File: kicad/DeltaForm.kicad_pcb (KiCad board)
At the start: 2 copper layers, 85.4 x 128.6 mm, 66 parts

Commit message: added MCU
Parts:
- moved D1 270.0 mm to (443.8, 98.5)
- moved D10 270.0 mm to (462.9, 141.4)
- moved D11 270.0 mm to (481.9, 141.4)
- moved D12 270.0 mm to (443.8, 160.4)
- moved D13 270.0 mm to (462.9, 160.4)
- moved D14 270.0 mm to (481.9, 160.4)
- moved D15 270.0 mm to (443.8, 179.5)
- moved D16 270.0 mm to (462.9, 179.5)
- moved D17 270.0 mm to (481.9, 179.5)
- moved D18 270.0 mm to (481.9, 198.5)
- moved D19 270.0 mm to (500.9, 150.9)
- moved D2 270.0 mm to (443.8, 122.3)
- moved D20 270.0 mm to (500.9, 189.0)
- moved D21 270.0 mm to (453.3, 198.5)
- moved D3 270.0 mm to (462.9, 98.5)
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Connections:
- S1 pad 1: col_3 -> Net-(D1-A)
- S1 pad 2: Net-(D1-A) -> col_3
- S10 pad 1: col_4 -> Net-(D10-A)
- S10 pad 2: Net-(D10-A) -> col_4
- S11 pad 1: col_5 -> Net-(D11-A)
- S11 pad 2: Net-(D11-A) -> col_5
- S12 pad 1: col_3 -> Net-(D12-A)
- S12 pad 2: Net-(D12-A) -> col_3
- S13 pad 1: col_4 -> Net-(D13-A)
- S13 pad 2: Net-(D13-A) -> col_4
- S14 pad 1: col_5 -> Net-(D14-A)
- S14 pad 2: Net-(D14-A) -> col_5
- S15 pad 1: col_3 -> Net-(D15-A)
- S15 pad 2: Net-(D15-A) -> col_3
- S16 pad 1: col_4 -> Net-(D16-A)
- S16 pad 2: Net-(D16-A) -> col_4
- S17 pad 1: col_5 -> Net-(D17-A)
- S17 pad 2: Net-(D17-A) -> col_5
- S18 pad 1: col_5 -> Net-(D18-A)
- S18 pad 2: Net-(D18-A) -> col_5
- S19 pad 1: col_6 -> Net-(D19-A)
- S19 pad 2: Net-(D19-A) -> col_6
- S2 pad 1: col_3 -> Net-(D2-A)
- S2 pad 2: Net-(D2-A) -> col_3
- S20 pad 1: col_6 -> Net-(D20-A)
- S20 pad 2: Net-(D20-A) -> col_6
- S21 pad 1: col_3 -> Net-(D21-A)
- S21 pad 2: Net-(D21-A) -> col_3
- S3 pad 1: col_4 -> Net-(D3-A)
- S3 pad 2: Net-(D3-A) -> col_4
- S4 pad 1: col_4 -> Net-(D4-A)
- S4 pad 2: Net-(D4-A) -> col_4
- S5 pad 1: col_5 -> Net-(D5-A)
- S5 pad 2: Net-(D5-A) -> col_5
- S6 pad 1: col_5 -> Net-(D6-A)
- S6 pad 2: Net-(D6-A) -> col_5
- S7 pad 1: col_6 -> Net-(D7-A)
- S7 pad 2: Net-(D7-A) -> col_6
- S8 pad 1: col_6 -> Net-(D8-A)
- S8 pad 2: Net-(D8-A) -> col_6
- S9 pad 1: col_3 -> Net-(D9-A)
- S9 pad 2: Net-(D9-A) -> col_3
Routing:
- net GND: track 0.00 -> 441.7 mm, vias 0 -> 12
- net VCC: track 0.00 -> 429.4 mm, vias 0 -> 3
- net col_3: track 0.00 -> 123.9 mm
- net col_5: track 0.00 -> 116.8 mm
- net col_6: track 0.00 -> 102.1 mm
- net col_4: track 0.00 -> 98.7 mm
- net row_16: track 0.00 -> 80.2 mm, vias 0 -> 1
- net row_14: track 0.00 -> 73.5 mm, vias 0 -> 1
- net row_12: track 0.00 -> 61.0 mm
- net row_13: track 0.00 -> 42.2 mm
- net row_15: track 0.00 -> 21.9 mm
- net Net-(D17-A): track 0.00 -> 7.79 mm
- net Net-(D11-A): track 0.00 -> 7.79 mm
- net Net-(D6-A): track 0.00 -> 7.79 mm
- net Net-(D5-A): track 0.00 -> 7.79 mm
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
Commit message: updated MCU
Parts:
- D1, D10, D11, D12, D13, D14, D15, D16, D17, D18, D19, D2, D20, D21, D3, D4, D5, D6, D7, D8, D9: value 1N4148W -> (none)
- S1, S10, S11, S12, S13, S14, S15, S16, S17, S18, S19, S2, S20, S3, S4, S5, S6, S7, S8, S9: value SW_MX_HS -> (none)
- S21: value SW_MX_HS -> (none); footprint TB2086_KEYSWITCH:SW_MX_HS_2u -> TB2086_KEYSWITCH:SW_MX_HS_1u
- STB1, STB2, STB3: value MX_stab -> Stabilizer_Cherry_MX_2.00u
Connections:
- net Net-(D1-A) renamed c17_func
- net Net-(D10-A) renamed c18_top
- net Net-(D11-A) renamed c19_top
- net Net-(D12-A) renamed c17_home
- net Net-(D13-A) renamed c18_home
- net Net-(D14-A) renamed c19_home
- net Net-(D15-A) renamed c17_bottom
- net Net-(D16-A) renamed c18_bottom
- net Net-(D17-A) renamed c19_bottom
- net Net-(D18-A) renamed c18_thumb
- net Net-(D19-A) renamed c20_top
- net Net-(D2-A) renamed c17_number
- net Net-(D20-A) renamed c20_bottom
- net Net-(D21-A) renamed c17_thumb
- net Net-(D3-A) renamed c18_func
- net Net-(D4-A) renamed c18_number
- net Net-(D5-A) renamed c19_func
- net Net-(D6-A) renamed c19_number
- net Net-(D7-A) renamed c20_func
- net Net-(D8-A) renamed c20_number
- net Net-(D9-A) renamed c17_top
- net row_12 renamed function
- net row_13 renamed number
- net row_14 renamed top
- net row_15 renamed home
- net row_16 renamed bottom
- net row_17 renamed thumb
- S1 pad 2: col_3 -> col_1
- S10 pad 2: col_4 -> col_1
- S11 pad 2: col_5 -> col_4
- S12 pad 2: col_3 -> col_1
- S13 pad 2: col_4 -> col_1
- S14 pad 2: col_5 -> col_4
- S15 pad 2: col_3 -> col_1
- S16 pad 2: col_4 -> col_1
- S17 pad 2: col_5 -> col_4
- S18 pad 2: col_5 -> col_1
- S19 pad 2: col_6 -> col_3
- S2 pad 2: col_3 -> col_1
- S20 pad 2: col_6 -> col_3
- S21 pad 2: col_3 -> col_1
- S3 pad 2: col_4 -> col_1
- S4 pad 2: col_4 -> col_1
- S5 pad 2: col_5 -> col_4
- S6 pad 2: col_5 -> col_4
- S7 pad 2: col_6 -> col_3
- S8 pad 2: col_6 -> col_3
- S9 pad 2: col_3 -> col_1
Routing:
- net GND: track 441.7 -> 0.00 mm, vias 12 -> 0
- net VCC: track 429.4 -> 0.00 mm, vias 3 -> 0
- net col_3: track 123.9 -> 0.00 mm
- net col_5: track 116.8 -> 0.00 mm
- net col_6: track 102.1 -> 0.00 mm
- net col_4: track 98.7 -> 0.00 mm
- net bottom: track 80.2 -> 0.00 mm, vias 1 -> 0
- net top: track 73.5 -> 0.00 mm, vias 1 -> 0
- net function: track 61.0 -> 0.00 mm
- net number: track 42.2 -> 0.00 mm
- net home: track 21.9 -> 0.00 mm
- net c19_top: track 7.79 -> 0.00 mm
- net c19_bottom: track 7.79 -> 0.00 mm
- net c19_number: track 7.79 -> 0.00 mm
- net c19_func: track 7.79 -> 0.00 mm
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
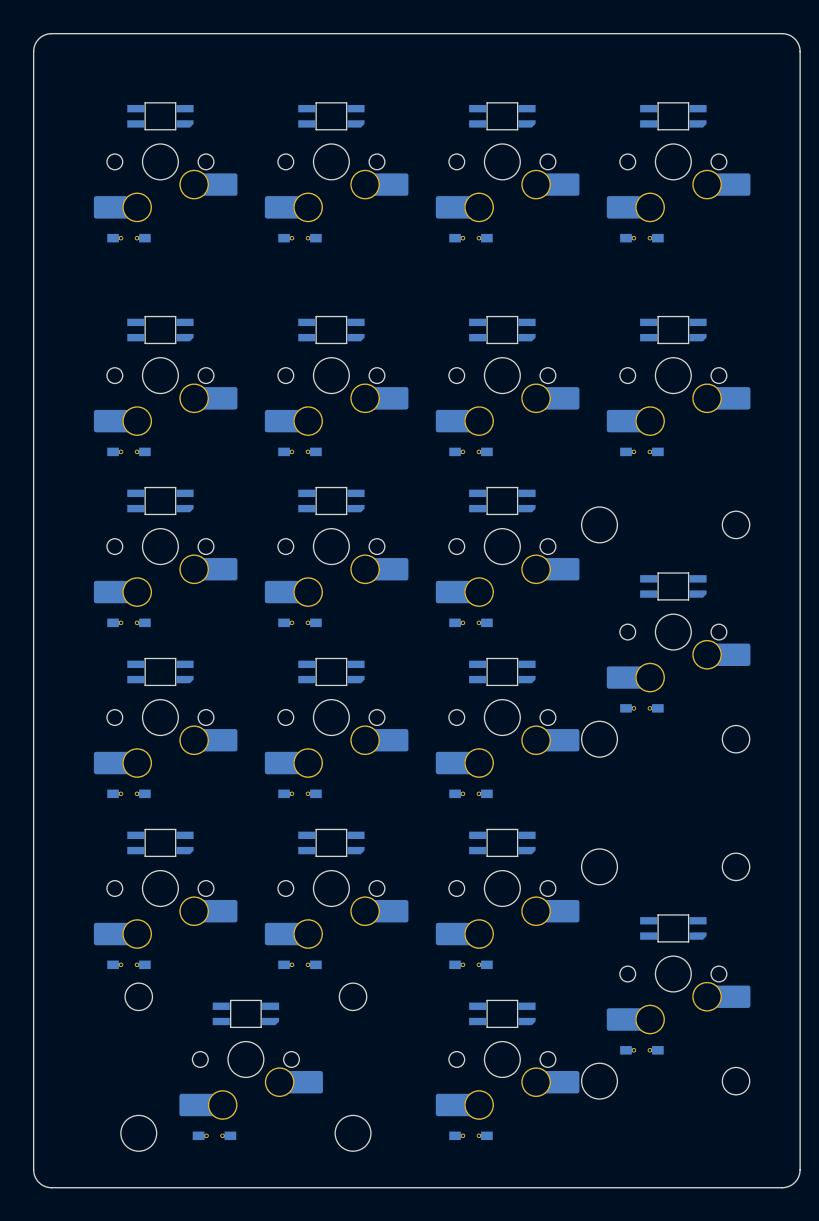
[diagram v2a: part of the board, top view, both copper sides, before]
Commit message: screw holes
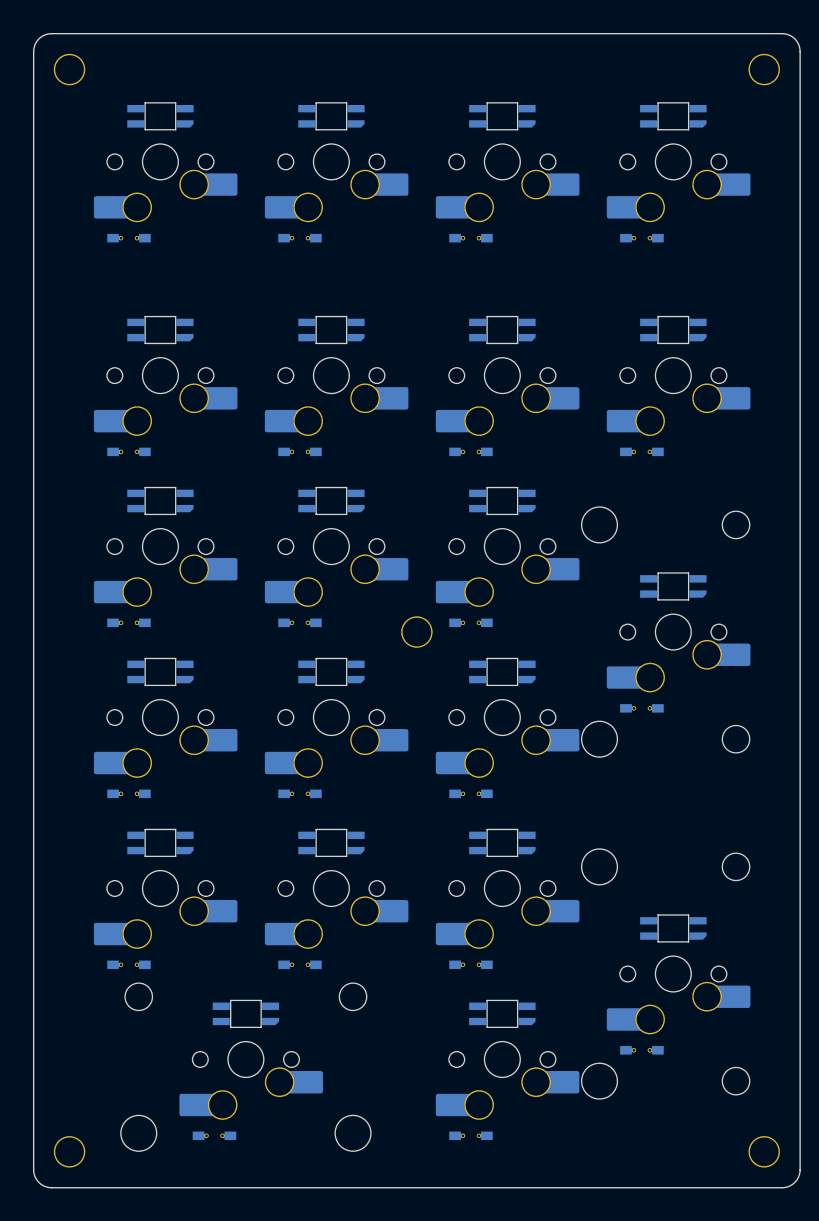
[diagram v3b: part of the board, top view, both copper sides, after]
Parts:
- added H1: MountingHole_3.2mm_Pad, TB2086_MISC:MountingHole_3.2mm_Pad, F.Cu at (437.2, 79.7)
- added H2: MountingHole_3.2mm_Pad, TB2086_MISC:MountingHole_3.2mm_Pad, F.Cu at (514.6, 79.7)
- added H3: MountingHole_3.2mm_Pad, TB2086_MISC:MountingHole_3.2mm_Pad, F.Cu at (514.6, 200.3)
- added H4: MountingHole_3.2mm_Pad, TB2086_MISC:MountingHole_3.2mm_Pad, F.Cu at (437.2, 200.3)
- added H5: MountingHole_3.2mm_Pad, TB2086_MISC:MountingHole_3.2mm_Pad, F.Cu at (475.9, 142.4)
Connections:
- net c18_thumb renamed c19_thumb

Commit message: pogo pin - ergogen
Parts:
- added POGO1: Pogopin_1x05_P2.54mm_Curved, TB2086_MISC:Pogopin_1x05_P2.54mm_Curved, B.Cu at (167.3, 95.5)
- added POGO2: Pogopin_1x05_P2.54mm_Curved, TB2086_MISC:Pogopin_1x05_P2.54mm_Curved, B.Cu at (244.4, 95.5)
- added POGO3: Pogopin_1x07_P2.54mm_Curved, TB2086_MISC:Pogopin_1x07_P2.54mm_Curved, B.Cu at (167.3, 142.4)
- added POGO4: Pogopin_1x07_P2.54mm_Curved, TB2086_MISC:Pogopin_1x07_P2.54mm_Curved, B.Cu at (244.4, 142.4)
- added POGO5: Pogopin_1x07_P2.54mm_Curved, TB2086_MISC:Pogopin_1x07_P2.54mm_Curved, B.Cu at (167.3, 182.0)
- added POGO6: Pogopin_1x07_P2.54mm_Curved, TB2086_MISC:Pogopin_1x07_P2.54mm_Curved, B.Cu at (244.4, 182.0)
- moved D10 270.0 mm to (192.8, 141.4)
- moved D11 270.0 mm to (211.9, 141.4)
- moved D13 270.0 mm to (192.8, 160.4)
- moved D14 270.0 mm to (211.9, 160.4)
- moved D16 270.0 mm to (192.8, 179.5)
- moved D17 270.0 mm to (211.9, 179.5)
- moved D18 270.0 mm to (211.9, 198.5)
- moved D3 270.0 mm to (192.8, 98.5)
- moved D4 270.0 mm to (192.8, 122.3)
- moved D5 270.0 mm to (211.9, 98.5)
- moved D6 270.0 mm to (211.9, 122.3)
- moved L10 270.0 mm to (196.3, 127.8)
- moved L11 270.0 mm to (215.4, 127.8)
- moved L13 270.0 mm to (196.3, 146.8)
- moved L14 270.0 mm to (215.4, 146.8)
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
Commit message: artwork for DeltaForm
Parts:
- added JP1: SolderJumper_2_Open, TB2086_MISC:SolderJumper-2_P1.3mm_Open_TrianglePad1.0x1.5mm, B.Cu at (167.8, 123.4)
- added JP2: SolderJumper_2_Open, TB2086_MISC:SolderJumper-2_P1.3mm_Open_TrianglePad1.0x1.5mm, B.Cu at (244.0, 123.3)
- added LED1: GREEN, LED_SMD:LED_0603_1608Metric_Pad1.05x0.95mm_HandSolder, F.Cu at (177.3, 101.5)
- added R1: 330, Resistor_SMD:R_0603_1608Metric, B.Cu at (177.3, 101.5)
- D1, D10, D11, D12, D13, D14, D15, D16, D17, D18, D19, D2, D20, D21, D3, D4, D5, D6, D7, D8, D9: value (none) -> 1N4148W
- L1, L10, L11, L12, L13, L14, L15, L16, L17, L18, L19, L2, L20, L21, L3, L4, L5, L6, L7, L8, L9: value TB2086_LED:LED_SK6812MINI-E -> SK6812MINI-E; footprint TB2086_LED:LED_SK6812MINI-E -> TB2086_LED_G:LED_SK6812MINI-E
- POGO1, POGO2: value Pogopin_1x05_P2.54mm_Curved -> Conn_01x05
- POGO3, POGO4, POGO5, POGO6: value Pogopin_1x07_P2.54mm_Curved -> Conn_01x07
- S1, S10, S11, S12, S13, S14, S15, S16, S17, S18, S19, S2, S20, S3, S4, S5, S6, S7, S8, S9: value (none) -> SW_MX_HS
- S21: value (none) -> SW_MX_HS; footprint TB2086_KEYSWITCH:SW_MX_HS_1u -> TB2086_KEYSWITCH:SW_MX_HS_2u
- STB1, STB2, STB3: value Stabilizer_Cherry_MX_2.00u -> MX_stab
- turned L1 to 180 degrees
- turned L10 to 180 degrees
- turned L13 to 180 degrees
- turned L15 to 180 degrees
- turned L16 to 180 degrees
- turned L19 to 180 degrees
- turned L20 to 180 degrees
- turned L3 to 180 degrees
- turned L4 to 180 degrees
- turned L5 to 180 degrees
- turned L7 to 180 degrees
- turned L8 to 180 degrees
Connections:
- net c17_bottom renamed Net-(D15-A)
- net c17_func renamed Net-(D1-A)
- net c17_home renamed Net-(D12-A)
- net c17_number renamed Net-(D2-A)
- net c17_thumb renamed Net-(D21-A)
- net c17_top renamed Net-(D9-A)
- net c18_bottom renamed Net-(D16-A)
- net c18_func renamed Net-(D3-A)
- net c18_home renamed Net-(D13-A)
- net c18_number renamed Net-(D4-A)
- net c18_top renamed Net-(D10-A)
- net c19_bottom renamed Net-(D17-A)
- net c19_func renamed Net-(D5-A)
- net c19_home renamed Net-(D14-A)
- net c19_number renamed Net-(D6-A)
- net c19_thumb renamed Net-(D18-A)
- net c19_top renamed Net-(D11-A)
- net c20_bottom renamed Net-(D20-A)
- net c20_func renamed Net-(D7-A)
- net c20_number renamed Net-(D8-A)
- net c20_top renamed Net-(D19-A)
- D1 pad 1: function -> ROW12
- D10 pad 1: top -> ROW14
- D11 pad 1: top -> ROW14
- D12 pad 1: home -> ROW15
- D13 pad 1: home -> ROW15
- D14 pad 1: home -> ROW15
- D15 pad 1: bottom -> ROW16
- D16 pad 1: bottom -> ROW16
- D17 pad 1: bottom -> ROW16
- D18 pad 1: thumb -> ROW17
- D19 pad 1: top -> ROW14
- D2 pad 1: number -> ROW13
- D20 pad 1: bottom -> ROW16
- D21 pad 1: thumb -> ROW17
- D3 pad 1: function -> ROW12
- D4 pad 1: number -> ROW13
- D5 pad 1: function -> ROW12
- D6 pad 1: number -> ROW13
- D7 pad 1: function -> ROW12
- D8 pad 1: number -> ROW13
- D9 pad 1: top -> ROW14
- L1 pad 1: VCC -> +5V
- L1 pad 2: (no net) -> Net-(L1-DOUT)
- L1 pad 4: (no net) -> RGB_FOM_LEFT
- L10 pad 1: VCC -> +5V
- L10 pad 2: (no net) -> Net-(L10-DOUT)
- L10 pad 4: (no net) -> Net-(L10-DIN)
- L11 pad 1: VCC -> +5V
- L11 pad 2: (no net) -> Net-(L11-DOUT)
- L11 pad 4: (no net) -> Net-(L11-DIN)
- L12 pad 1: VCC -> +5V
- L12 pad 2: (no net) -> Net-(L12-DOUT)
- L12 pad 4: (no net) -> Net-(L12-DIN)
- L13 pad 1: VCC -> +5V
- L13 pad 2: (no net) -> Net-(L10-DIN)
- L13 pad 4: (no net) -> Net-(L13-DIN)
- L14 pad 1: VCC -> +5V
- L14 pad 2: (no net) -> Net-(L14-DOUT)
- L14 pad 4: (no net) -> Net-(L11-DOUT)
- L15 pad 1: VCC -> +5V
- L15 pad 2: (no net) -> Net-(L15-DOUT)
- L15 pad 4: (no net) -> Net-(L12-DOUT)
- L16 pad 1: VCC -> +5V
- L16 pad 2: (no net) -> Net-(L13-DIN)
- L16 pad 4: (no net) -> Net-(L15-DOUT)
- L17 pad 1: VCC -> +5V
- L17 pad 2: (no net) -> Net-(L17-DOUT)
- L17 pad 4: (no net) -> Net-(L14-DOUT)
- L18 pad 1: VCC -> +5V
- L18 pad 2: (no net) -> Net-(L18-DOUT)
- L18 pad 4: (no net) -> RGB_FOM_RIGHT
- L19 pad 1: VCC -> +5V
- L19 pad 2: (no net) -> Net-(L19-DOUT)
- L19 pad 4: (no net) -> Net-(L19-DIN)
- L2 pad 1: VCC -> +5V
- L2 pad 2: (no net) -> Net-(L2-DOUT)
- L2 pad 4: (no net) -> Net-(L1-DOUT)
- L20 pad 1: VCC -> +5V
- L20 pad 2: (no net) -> Net-(L19-DIN)
- L20 pad 4: (no net) -> Net-(L17-DOUT)
- L21 pad 1: VCC -> +5V
- L21 pad 2: (no net) -> RGB_TO_LEFT
- L21 pad 4: (no net) -> Net-(L18-DOUT)
- L3 pad 1: VCC -> +5V
- L3 pad 2: (no net) -> Net-(L3-DOUT)
- L3 pad 4: (no net) -> Net-(L3-DIN)
- L4 pad 1: VCC -> +5V
- L4 pad 2: (no net) -> Net-(L3-DIN)
- L4 pad 4: (no net) -> Net-(L10-DOUT)
- L5 pad 1: VCC -> +5V
- L5 pad 2: (no net) -> Net-(L5-DOUT)
- L5 pad 4: (no net) -> Net-(L3-DOUT)
- L6 pad 1: VCC -> +5V
- L6 pad 2: (no net) -> Net-(L11-DIN)
- L6 pad 4: (no net) -> Net-(L5-DOUT)
- L7 pad 1: VCC -> +5V
- L7 pad 2: (no net) -> RGB_TO_RIGHT
- L7 pad 4: (no net) -> Net-(L7-DIN)
- L8 pad 1: VCC -> +5V
- L8 pad 2: (no net) -> Net-(L7-DIN)
- L8 pad 4: (no net) -> Net-(L19-DOUT)
- L9 pad 1: VCC -> +5V
- L9 pad 2: (no net) -> Net-(L12-DIN)
- L9 pad 4: (no net) -> Net-(L2-DOUT)
- POGO1 pad 1: P1 -> RGB_FOM_LEFT
- POGO1 pad 2: P2 -> SCR
- POGO1 pad 3: P3 -> NUM
- POGO1 pad 4: P4 -> +5V
- POGO1 pad 5: P5 -> GND
- POGO2 pad 1: P1 -> GND
- POGO2 pad 2: P2 -> +5V
- POGO2 pad 3: P3 -> NUM
- POGO2 pad 4: P4 -> SCR
- POGO2 pad 5: P5 -> RGB_TO_RIGHT
- POGO3 pad 1: P1 -> COL0
- POGO3 pad 2: P2 -> COL1
- POGO3 pad 3: P3 -> COL2
- POGO3 pad 4: P4 -> COL3
- POGO3 pad 5: P5 -> COL4
- POGO3 pad 6: P6 -> COL5
- POGO3 pad 7: P7 -> COL6
- POGO4 pad 1: P1 -> COL6
- POGO4 pad 2: P2 -> COL5
- POGO4 pad 3: P3 -> COL4
- POGO4 pad 4: P4 -> COL3
- POGO4 pad 5: P5 -> COL2
- POGO4 pad 6: P6 -> COL1
- POGO4 pad 7: P7 -> COL0
- POGO5 pad 1: P1 -> ROW12
- POGO5 pad 2: P2 -> ROW13
- POGO5 pad 3: P3 -> ROW14
- POGO5 pad 4: P4 -> ROW15
- POGO5 pad 5: P5 -> ROW16
- POGO5 pad 6: P6 -> ROW17
- POGO5 pad 7: P7 -> RGB_TO_LEFT
- POGO6 pad 1: P1 -> RGB_FOM_RIGHT
- POGO6 pad 2: P2 -> ROW17
- POGO6 pad 3: P3 -> ROW16
- POGO6 pad 4: P4 -> ROW15
- POGO6 pad 5: P5 -> ROW14
- POGO6 pad 6: P6 -> ROW13
- POGO6 pad 7: P7 -> ROW12
- S1 pad 2: col_1 -> COL3
- S10 pad 2: col_1 -> COL4
- S11 pad 2: col_4 -> COL5
- S12 pad 2: col_1 -> COL3
- S13 pad 2: col_1 -> COL4
- S14 pad 2: col_4 -> COL5
- S15 pad 2: col_1 -> COL3
- S16 pad 2: col_1 -> COL4
- S17 pad 2: col_4 -> COL5
- S18 pad 2: col_1 -> COL5
- S19 pad 2: col_3 -> COL6
- S2 pad 2: col_1 -> COL3
- S20 pad 2: col_3 -> COL6
- S21 pad 2: col_1 -> COL3
- S3 pad 2: col_1 -> COL4
- S4 pad 2: col_1 -> COL4
- S5 pad 2: col_4 -> COL5
- S6 pad 2: col_4 -> COL5
- S7 pad 2: col_3 -> COL6
- S8 pad 2: col_3 -> COL6
- S9 pad 2: col_1 -> COL3
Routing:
- net +5V: track 0.00 -> 506.3 mm, vias 0 -> 3
- net ROW12: track 0.00 -> 227.7 mm, vias 0 -> 2
- net COL3: track 0.00 -> 220.4 mm, vias 0 -> 2
- net COL5: track 0.00 -> 207.4 mm
- net COL6: track 0.00 -> 205.8 mm, vias 0 -> 3
- net COL4: track 0.00 -> 184.1 mm, vias 0 -> 1
- net ROW13: track 0.00 -> 180.6 mm, vias 0 -> 3
- net ROW14: track 0.00 -> 149.0 mm, vias 0 -> 2
- net ROW15: track 0.00 -> 110.7 mm, vias 0 -> 1
- net ROW17: track 0.00 -> 99.6 mm
- net RGB_FOM_RIGHT: track 0.00 -> 96.1 mm, vias 0 -> 1
- net NUM: track 0.00 -> 94.2 mm
- net COL0: track 0.00 -> 93.4 mm, vias 0 -> 2
- net ROW16: track 0.00 -> 93.2 mm, vias 0 -> 2
- net COL1: track 0.00 -> 90.9 mm, vias 0 -> 3
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
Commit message: Silk Screen
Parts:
- added G***: LOGO, omnicode-9001:OmniCode-9001, F.Cu at (204.4, 101.8)
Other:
- board text added: "DeltaForm"
- board text added: "OmniCode:9001 - 202507.01"
- board text added: "OmniCode:9001 - DeltaForm"

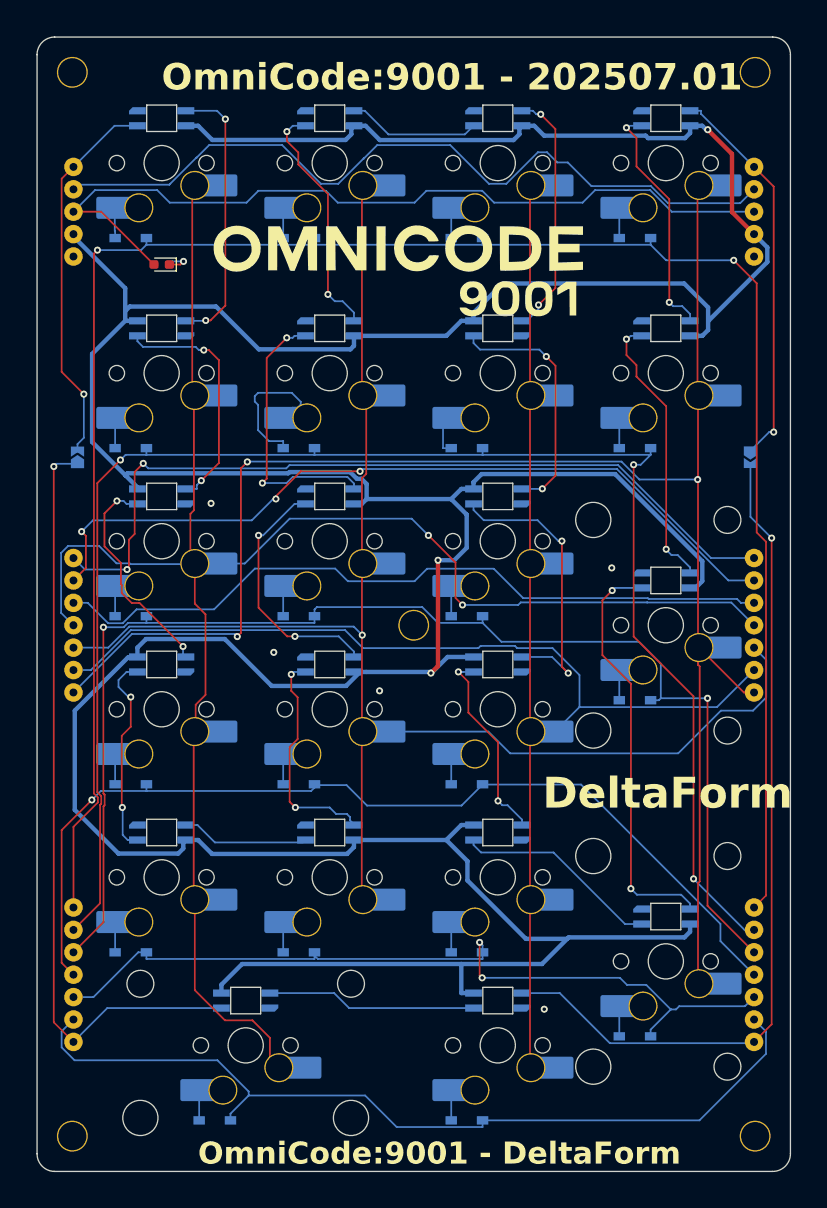
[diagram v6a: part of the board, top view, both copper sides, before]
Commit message: changed screw sizes
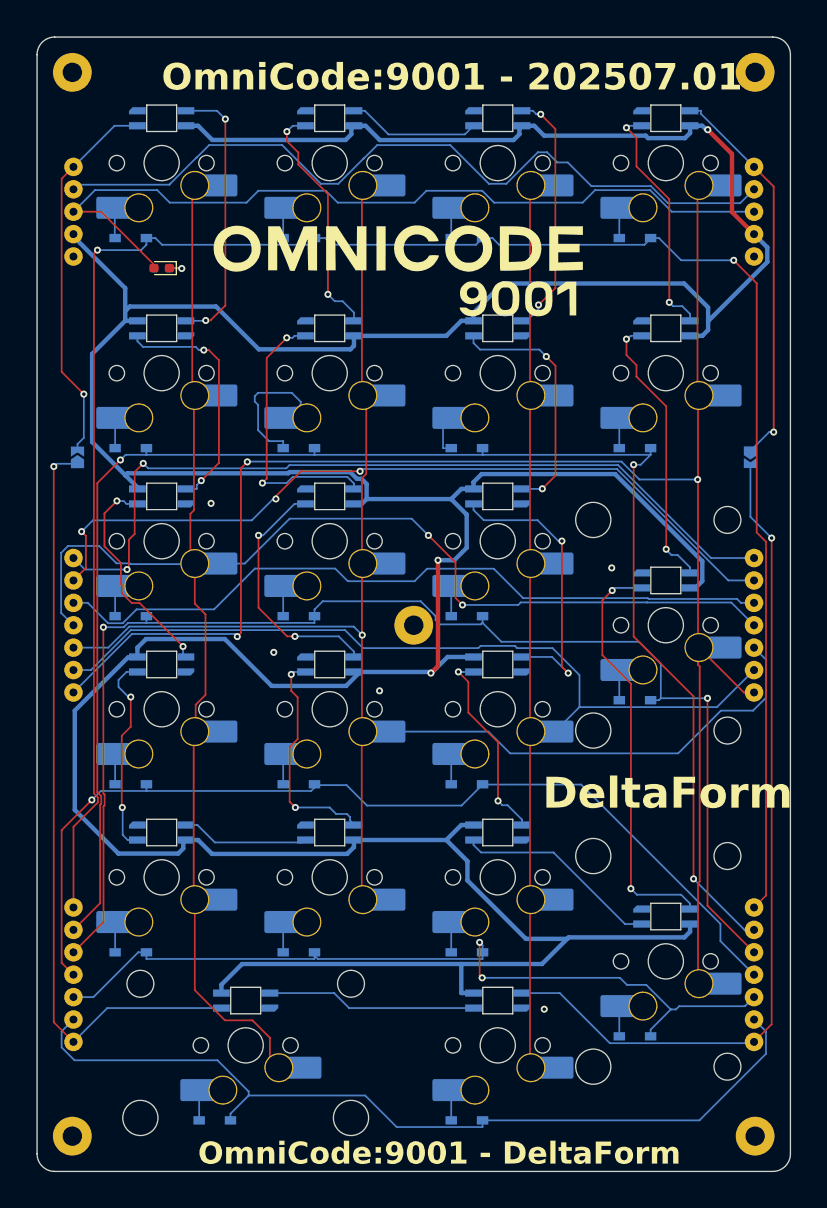
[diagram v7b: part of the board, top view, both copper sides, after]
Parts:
- H1, H2, H3, H4, H5: value MountingHole_3.2mm_Pad -> MountingHole_2.2mm_M2_Pad; footprint TB2086_MISC:MountingHole_3.2mm_Pad -> TB2086_MISC:MountingHole_2.2mm_M2_Pad
- moved LED1 0.41 mm to (177.3, 101.9)
- moved R1 0.41 mm to (177.3, 101.9)
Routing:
- net COL3: track 220.4 -> 215.0 mm
- net +5V: track 506.3 -> 504.7 mm
- net Net-(D4-A): track 19.7 -> 18.1 mm
- net COL5: track 207.4 -> 205.9 mm
- net COL4: track 184.1 -> 182.6 mm
- net Net-(D6-A): track 7.46 -> 6.20 mm
- net COL6: track 205.8 -> 204.8 mm
- net ROW14: track 149.0 -> 150.0 mm
- net SCR: track 89.3 -> 88.6 mm
- net Net-(L5-DOUT): track 28.3 -> 27.7 mm
